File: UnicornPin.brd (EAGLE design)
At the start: 61.6 x 52.1 mm, 6 parts

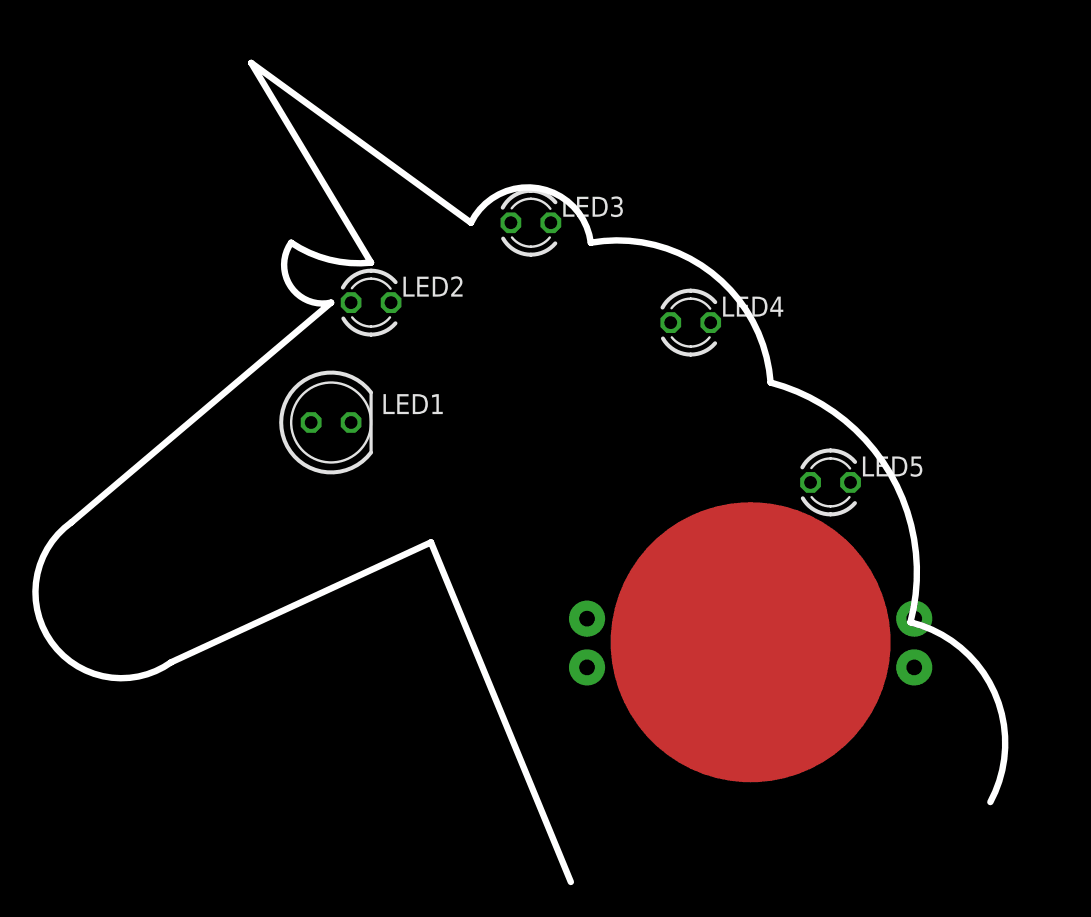
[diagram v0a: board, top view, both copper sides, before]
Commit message: modified unicorn board
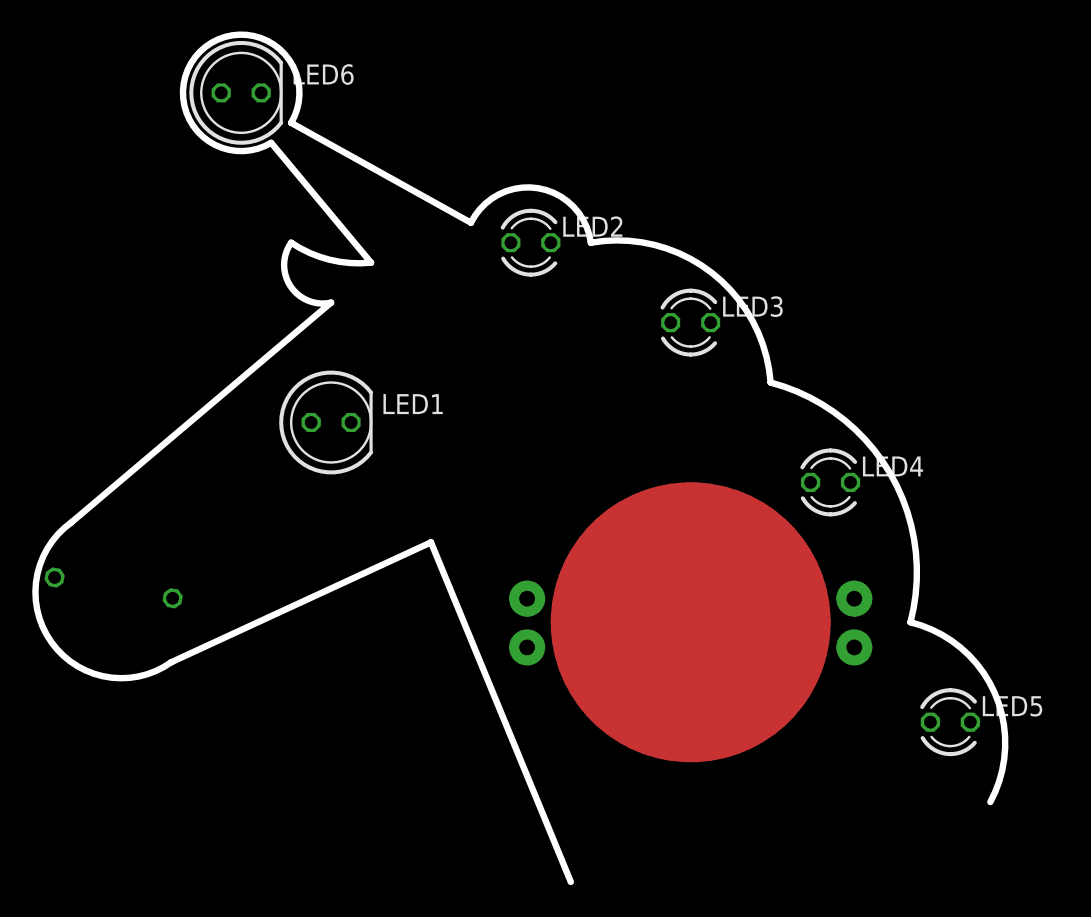
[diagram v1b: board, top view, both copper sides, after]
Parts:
- added LED6: (no value), led:LED5MM
- added R1: 120R, resistor:0207/7
- moved LED5 17.0 mm to (71.1, 34.3)
- moved LED4 13.5 mm to (63.5, 49.5)
- moved LED3 12.0 mm to (54.6, 59.7)
- moved LED2 10.9 mm to (44.5, 64.8)
- moved U$1 4.02 mm to (54.6, 40.6)
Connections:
- new net N$6: LED1.A, LED6.K
- new net N$7: R1.1, U$1.P$5
- net N$1: now also LED6.A, R1.2; no longer LED1.A, U$1.P$5
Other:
- board size 61.6 x 52.1 mm -> 61.6 x 53.9 mm

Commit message: added unicorn board
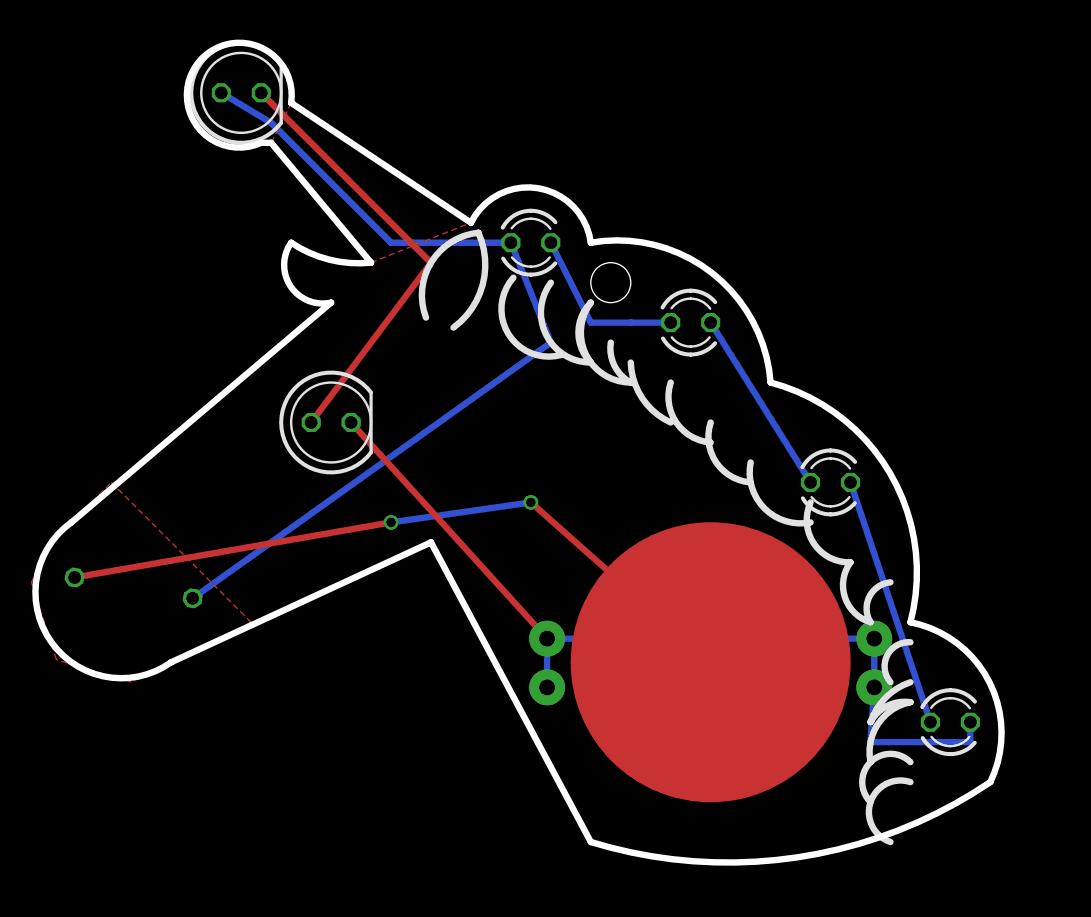
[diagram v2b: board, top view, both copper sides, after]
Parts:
- moved U$1 2.84 mm to (55.9, 38.1)
- moved R1 1.27 mm to (19.2, 42.8)
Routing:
- net N$1: track 0.00 -> 56.9 mm
- net N$2: track 0.00 -> 56.7 mm
- net N$7: track 0.00 -> 44.7 mm, vias 0 -> 2
- net N$6: track 0.00 -> 28.0 mm
- net N$5: track 0.00 -> 16.1 mm
- net N$4: track 0.00 -> 12.0 mm
- net N$3: track 0.00 -> 10.8 mm
- added copper zone on layer 1, net N$6
- added copper zone on layer 1, net N$7
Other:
- board size 61.6 x 53.9 mm -> 61.4 x 52.1 mm

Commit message: final unicorn design
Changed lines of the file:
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@@
 <layers>
 <layer number="1" name="Top" color="4" fill="1" visible="no" active="yes"/>
-<layer number="16" name="Bottom" color="1" fill="1" visible="no" active="yes"/>
-<layer number="17" name="Pads" color="2" fill="1" visible="no" active="yes"/>
-<layer number="18" name="Vias" color="2" fill="1" visible="no" active="yes"/>
-<layer number="19" name="Unrouted" color="6" fill="1" visible="no" active="yes"/>
+<layer number="16" name="Bottom" color="1" fill="1" visible="yes" active="yes"/>
+<layer number="17" name="Pads" color="2" fill="1" visible="yes" active="yes"/>
+<layer number="18" name="Vias" color="2" fill="1" visible="yes" active="yes"/>
+<layer number="19" name="Unrouted" color="6" fill="1" visible="yes" active="yes"/>
 <layer number="20" name="Dimension" color="15" fill="1" visible="yes" active="yes"/>
 <layer number="21" name="tPlace" color="7" fill="1" visible="yes" active="yes"/>
@@
 <wire x1="62.23" y1="48.26" x2="64.77" y2="44.45" width="0.4064" layer="21" curve="116.565051"/>
 <wire x1="64.77" y1="44.45" x2="66.04" y2="40.64" width="0.4064" layer="21" curve="109.653824"/>
-<wire x1="66.04" y1="40.64" x2="67.31" y2="43.18" width="0.4064" layer="21" curve="-116.565051"/>
 <wire x1="68.58" y1="39.37" x2="67.31" y2="36.83" width="0.4064" layer="21" curve="135"/>
 <wire x1="68.58" y1="36.83" x2="66.04" y2="34.29" width="0.4064" layer="21" curve="53.130102"/>
 <wire x1="66.04" y1="34.29" x2="68.58" y2="35.56" width="0.4064" layer="21" curve="-70.346176"/>
 <wire x1="68.58" y1="35.56" x2="66.04" y2="31.75" width="0.4064" layer="21" curve="90"/>
-<wire x1="67.31" y1="26.67" x2="68.58" y2="30.48" width="0.4064" layer="21" curve="-180"/>
-<wire x1="66.04" y1="29.21" x2="68.58" y2="31.75" width="0.4064" layer="21" curve="-180"/>
+<wire x1="31.75" y1="60.96" x2="33.655" y2="61.43625" width="0.4064" layer="21" curve="29.744881"/>
+<wire x1="33.02" y1="60.96" x2="37.1475" y2="61.75375" width="0.4064" layer="21" curve="87.49686"/>
+<wire x1="40.64" y1="60.96" x2="43.18" y2="58.42" width="0.4064" layer="21" curve="90"/>
+<wire x1="66.04" y1="40.64" x2="66.04" y2="41.91" width="0.4064" layer="21" curve="-21.801409"/>
+<wire x1="66.04" y1="29.21" x2="67.31" y2="31.75" width="0.4064" layer="21" curve="-135"/>
+<wire x1="66.04" y1="26.67" x2="66.51625" y2="29.845" width="0.4064" layer="21" curve="-86.82017"/>
 </plain>
 <attributes>
@@
 <contactref element="LED4" pad="K"/>
 <contactref element="LED5" pad="A"/>
+<wire x1="64.77" y1="49.53" x2="67.31" y2="41.91" width="0" layer="19" extent="1-16"/>
 <wire x1="64.77" y1="49.53" x2="69.85" y2="34.29" width="0.4064" layer="16"/>
+<wire x1="67.31" y1="40.64" x2="67.31" y2="41.91" width="0" layer="19" curve="-180" extent="1-16"/>
 </signal>
 <signal name="N$6">
